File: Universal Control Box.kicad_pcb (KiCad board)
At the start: 4 copper layers, 168.2 x 98.8 mm, 91 parts, among them J101 Conn_01x06, J102 Conn_01x07, J103 USB_C_Receptacle_USB2.0, U101 ESP32-WROOM-32, U102 PCF8575DBR (PCF1), U103 XC6220B331MR-G, U104 74AHCT1G125, U201 PEC11H-4025F-S0016, U202 PEC11H-4025F-S0016

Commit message: Updated PCB to include USB based RX/TX
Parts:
- removed J101: Conn_01x06, Connector_PinSocket_2.54mm:PinSocket_1x06_P2.54mm_Vertical
- removed L101: L_Ferrite_Small, Inductor_SMD:L_0603_1608Metric
- added C106: 10uF, Capacitor_SMD:C_0603_1608Metric, F.Cu at (102.5, 35.3)
- added C107: 100nF, Capacitor_SMD:C_0603_1608Metric, F.Cu at (103.3, 38.0)
- added C108: 100nF, Capacitor_SMD:C_0603_1608Metric, F.Cu at (92.0, 35.9)
- added C109: 1uF, Capacitor_SMD:C_0603_1608Metric, F.Cu at (92.3, 31.4)
- added C110: 100nF, Capacitor_SMD:C_0603_1608Metric, F.Cu at (93.9, 31.4)
- added D104: SP0503BAHT, Package_TO_SOT_SMD:SOT-143, F.Cu at (90.8, 41.5)
- added FB101: FerriteBead_Small, Resistor_SMD:R_0805_2012Metric, F.Cu at (99.0, 37.9)
- added Q101: MMDT3904, Package_TO_SOT_SMD:SOT-363_SC-70-6, F.Cu at (77.0, 36.6)
- added R107: 10K, Resistor_SMD:R_0603_1608Metric, F.Cu at (80.0, 39.0)
- added R108: 10K, Resistor_SMD:R_0603_1608Metric, F.Cu at (80.0, 34.2)
- added SW101: SW_Push, footprints:XKB-Connectivity-TS-1187A-B-A-B, F.Cu at (68.3, 25.9)
- added SW102: SW_Push, footprints:XKB-Connectivity-TS-1187A-B-A-B, F.Cu at (75.5, 25.9)
- added U105: CP2102-GMR, Package_DFN_QFN:QFN-28-1EP_5x5mm_P0.5mm_EP3.35x3.35mm, F.Cu at (86.1, 36.6)
- moved REF** 36.5 mm to (170.6, 32.4)
- moved C105 4.78 mm to (102.3, 42.9)
- moved U103 4.78 mm to (99.0, 41.7)
- moved C104 2.30 mm to (95.4, 36.6)
- moved F101 2.30 mm to (99.0, 33.1)
- moved REF** 0.97 mm to (137.4, 29.6)
- moved U201 0.10 mm to (118.2, 47.9)
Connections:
- F101 pad 2: +5V -> Net-(C106-Pad1)
- J103 pad A6: unconnected-(J103-D+-PadA6) -> /DATA_P
- J103 pad A7: unconnected-(J103-D--PadA7) -> /DATA_N
- J103 pad B6: unconnected-(J103-D+-PadB6) -> /DATA_P
- J103 pad B7: unconnected-(J103-D--PadB7) -> /DATA_N
- J103 pad S1: Net-(J103-SHIELD) -> GND
- U101 pad 26: unconnected-(U101-IO4-Pad26) -> /OLED_DC
- U101 pad 29: unconnected-(U101-IO5-Pad29) -> /OLED_CS
- U101 pad 6: /OLED_CS -> unconnected-(U101-IO34-Pad6)
- U101 pad 7: /OLED_DC -> unconnected-(U101-IO35-Pad7)
- U201 pad S1: GND -> +3.3V
- U202 pad S1: GND -> +3.3V
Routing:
- net /EN: track 38.3 -> 83.5 mm, vias 1 -> 4
- net GND: track 136.0 -> 175.3 mm, vias 57 -> 62
- net Net-(D104-K-Pad4): track 8.55 -> 33.3 mm, vias 0 -> 2
- net /DATA_P: track 0.00 -> 23.8 mm, vias 0 -> 3
- net /DATA_N: track 0.00 -> 23.5 mm, vias 0 -> 2
- net Net-(J103-SHIELD): track 19.5 -> 0.00 mm
- net /ESP_TX: track 37.4 -> 55.0 mm, vias 2 -> 3
- net /DTR: track 0.00 -> 17.1 mm
- net /RTS: track 0.00 -> 16.7 mm
- net +5V: track 201.0 -> 217.3 mm
- net /ESP_RX: track 20.8 -> 36.6 mm, vias 1 -> 2
- net /OLED_DC: track 20.6 -> 35.5 mm, vias 0 -> 2
- net /OLED_CS: track 22.3 -> 35.6 mm, vias 0 -> 2
- net Net-(Q101A-B1): track 0.00 -> 8.02 mm, vias 0 -> 2
- net Net-(Q101B-B2): track 0.00 -> 6.00 mm
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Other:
- board text added: "EN"
- board text added: "IO0"
- board text added: "SSD1309 OLED Display"
- board text added: "SW1"
- board text added: "SW10"
- board text added: "SW11"
- board text added: "SW13"
- board text added: "SW14"
- board text added: "SW15"
- board text added: "SW16"
- board text added: "SW17"
- board text added: "SW18"
- board text added: "SW19"
- board text added: "SW2"
- board text added: "SW20"
- board text added: "SW3"
- board text added: "SW4"
- board text added: "SW8"
- board text added: "SW9"

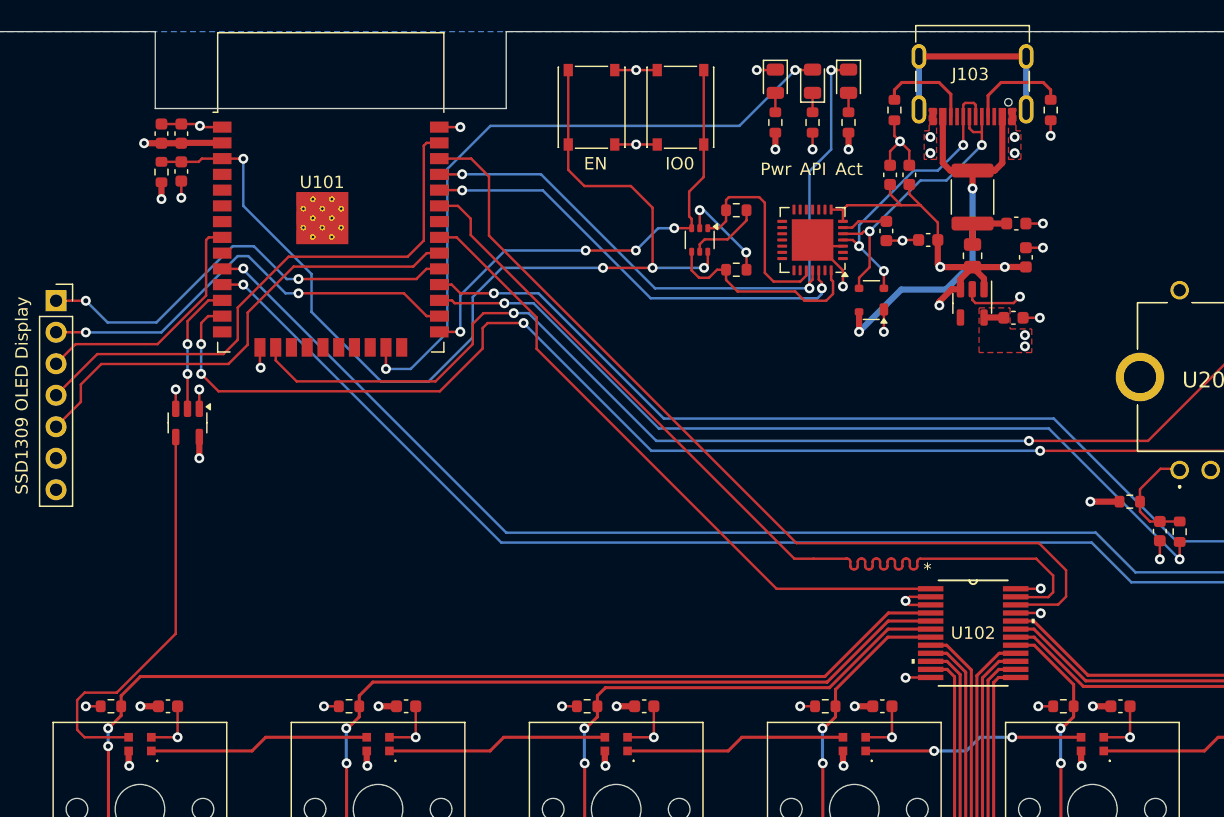
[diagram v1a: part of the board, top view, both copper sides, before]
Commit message: minor fixes
- moved some tracks
- vias to each ground pads
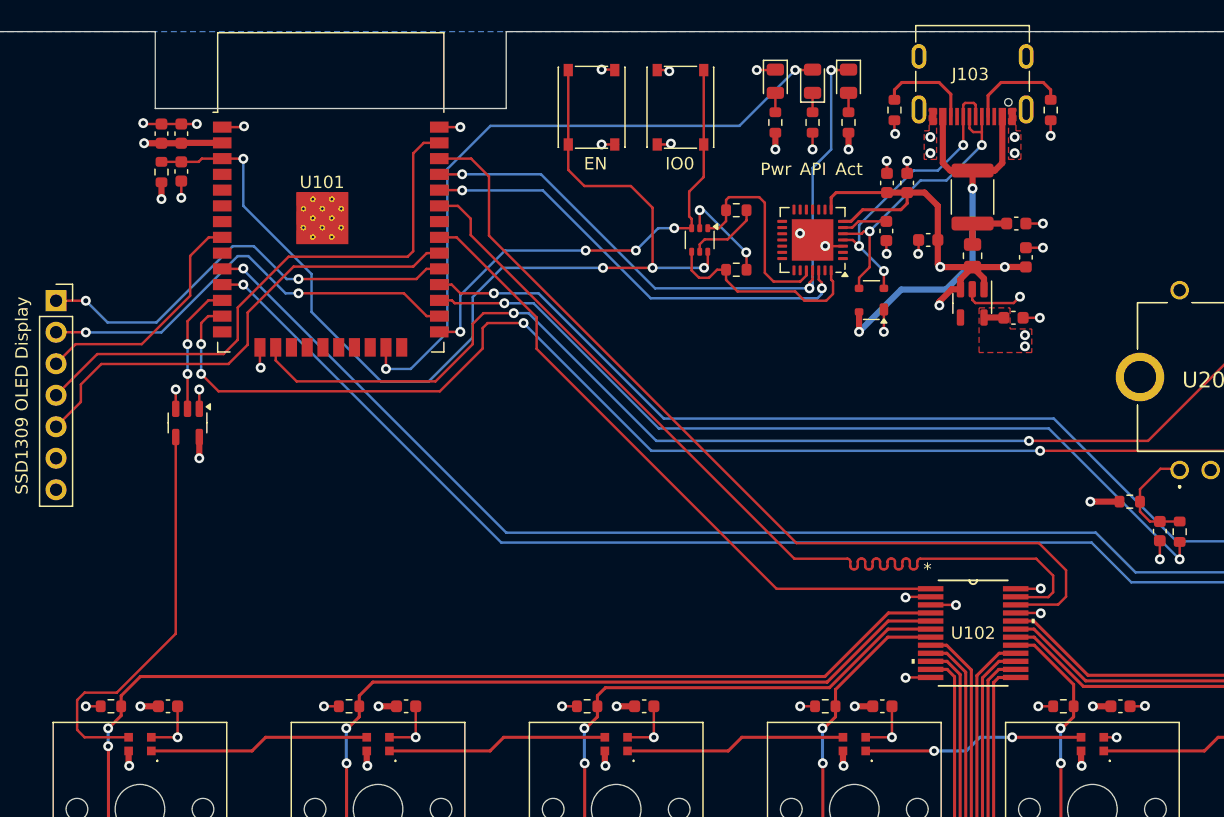
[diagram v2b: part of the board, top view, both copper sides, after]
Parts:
- moved C110 1.91 mm to (92.1, 32.0)
- moved C109 1.52 mm to (93.7, 32.0)
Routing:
- net GND: track 175.3 -> 146.6 mm, vias 62 -> 72
- net +5V: track 217.3 -> 221.1 mm
- net /OLED_RESET: track 20.2 -> 19.5 mm

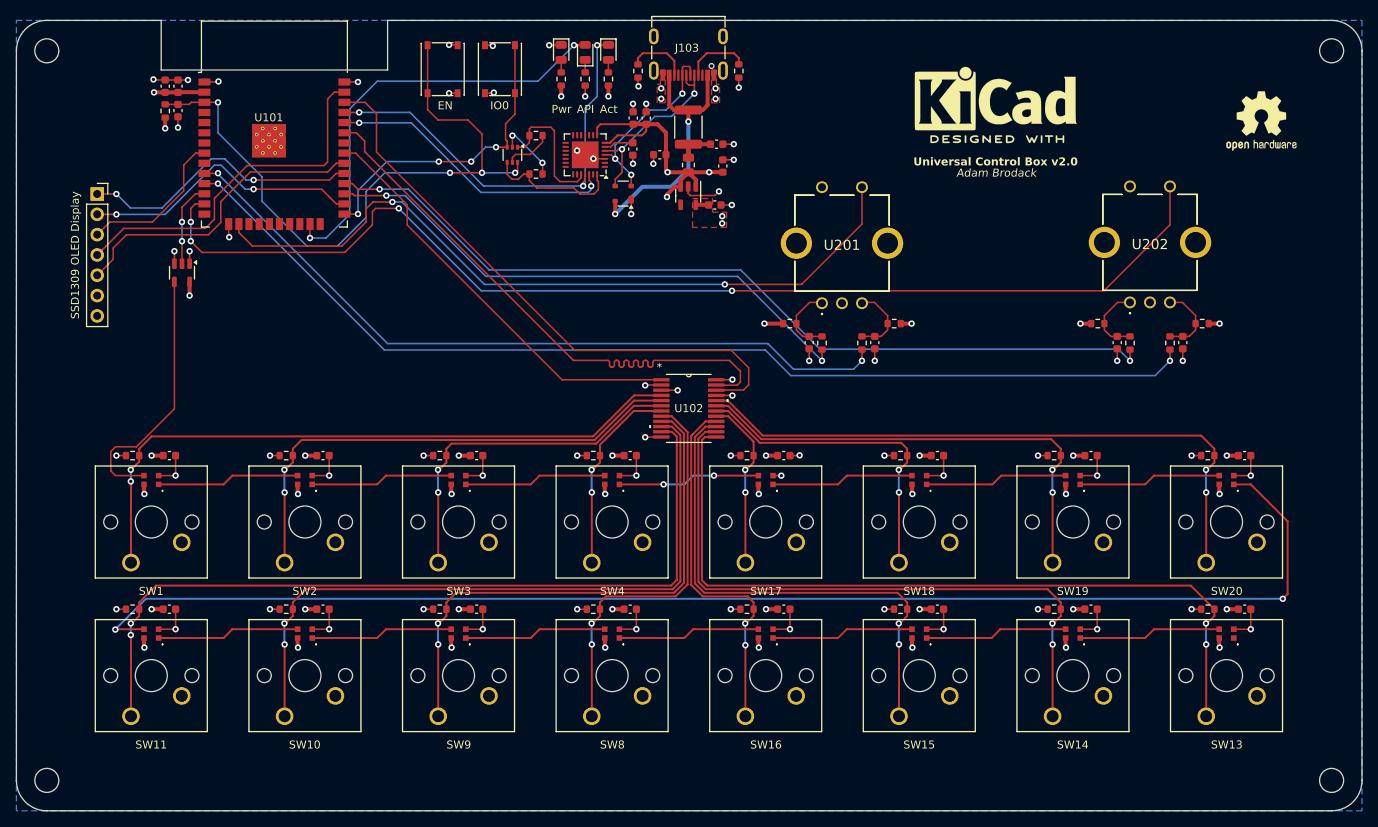
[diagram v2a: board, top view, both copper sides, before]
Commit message: Fixed GND positions & LCSC part for dual mosfet
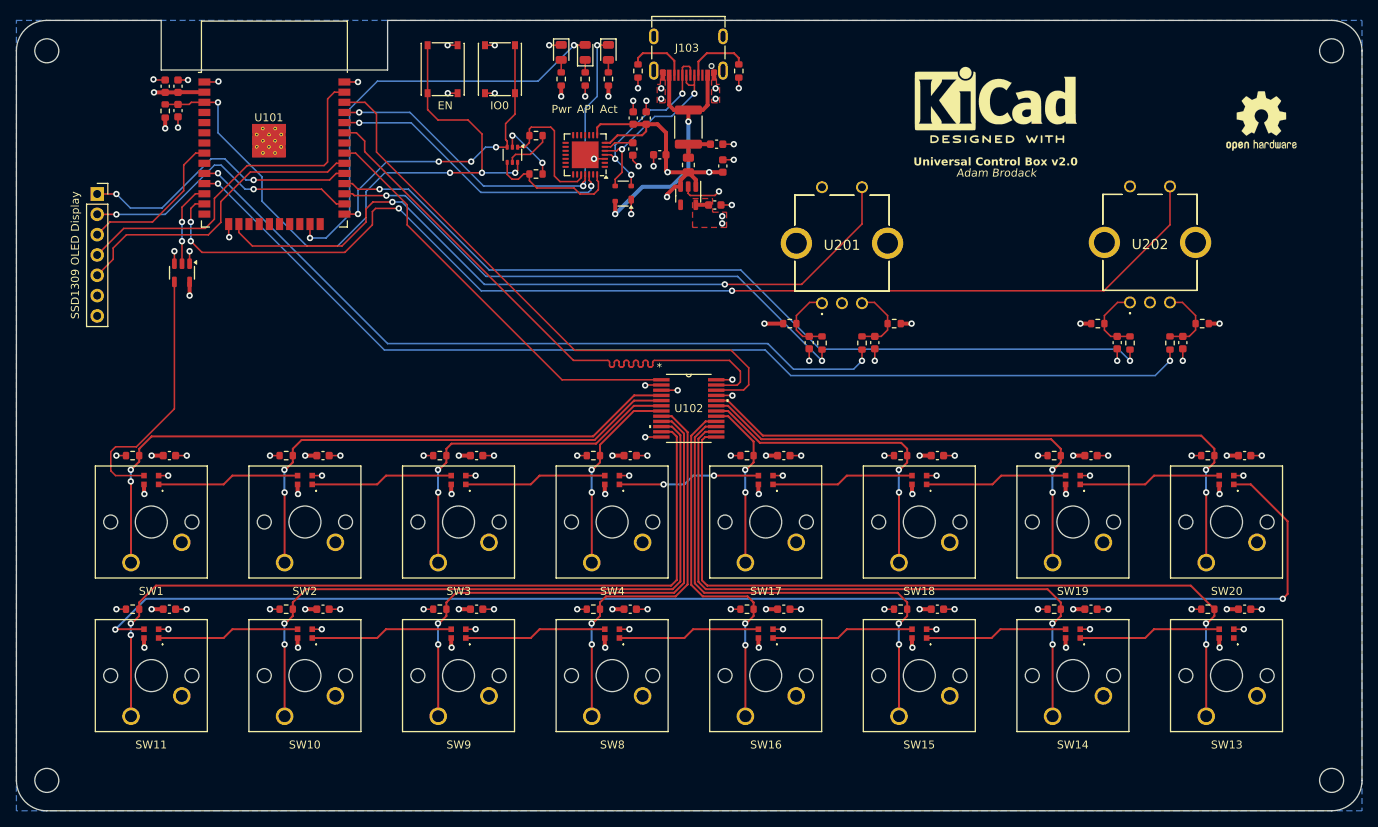
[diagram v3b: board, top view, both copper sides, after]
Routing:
- net GND: track 146.6 -> 117.6 mm, vias 72 -> 86
